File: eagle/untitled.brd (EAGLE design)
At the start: 50 x 50 mm, 48 parts, among them J1 JTAG, Q1 16MHz, U1 MMA3202KEG

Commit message: Update board.
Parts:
- removed D11: DIODE, gipi:1206
- removed G1: BAT, SparkFun-Electromechanical:BATTCOM_20MM_PTH
- added C7, C8, C9: 10nF, SparkFun-Capacitors:0603-CAP
- added D13: (no value), diode:SMB
- added JP6: M02JST-PTH-VERT, SparkFun-Connectors:JST-2-PTH-VERT
- added L1: (no value), SparkFun-Passives:0603
- added LED1: (no value), SparkFun-LED:LED-0603
- added R16, R17, R18: 1k, SparkFun-Passives:0603-RES
- added U$3: V_REG_TPS61040SMD, SparkFun-PowerIC:SOT23-5
- C1, C2, C3: device SparkFun-Capacitors:1206 -> SparkFun-Capacitors:0603-CAP
- C4, C5: value 10pF -> 10nF; device SparkFun-Capacitors:1206 -> SparkFun-Capacitors:0603-CAP
- GOLD_ORB_SM1: value OSHWLOGO_GOLD_ORB_SM -> OSHWLOGO_GOLD_ORB_LG; device bfl:OSHW2 -> bfl:OSHW0
- JP1: value M11PTH -> M13; device SparkFun-Connectors:1X11 -> SparkFun-Connectors:1X13
- R10, R3, R9: device SparkFun-Passives:1206 -> SparkFun-Passives:0603-RES
- moved J1 21.7 mm to (43.9, 75.4)
- moved C3 18.2 mm to (27.7, 75.5)
- moved U1 17.9 mm to (23.1, 73.4), flipped to the bottom, turned to 270 degrees
- moved JP5 14.4 mm to (9.75, 47.4), turned to 0 degrees
- moved GOLD_ORB_SM1 13.8 mm to (40.0, 46.0)
- moved SJ1 11.4 mm to (18.7, 72.9), turned to 270 degrees
- moved C5 11.2 mm to (30.1, 71.0), turned to 270 degrees
- moved JP2 10.9 mm to (5.29, 60.2)
- moved D12 9.81 mm to (11.9, 52.8), flipped to the bottom, turned to 180 degrees
- moved S1 8.30 mm to (4.40, 76.8)
- moved C6 8.06 mm to (13.2, 56.7)
- moved R9 7.30 mm to (27.9, 71.0)
- moved R1 6.33 mm to (13.2, 61.0)
- moved R2 6.29 mm to (13.3, 63.6)
- moved C4 4.13 mm to (25.7, 71.0), turned to 270 degrees
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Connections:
- removed net N$33: D11.P$1, G1.2
- new net GN: C4.1, C5.1, C6.2, D1.C, D2.C, D3.C, D4.C, D5.C, D6.C, D7.C, D8.C, D9.C, J1.10, J1.2, JP1.12, JP5.6, LED1.C, S1.1, S1.2, S2.3
- new net N$35: R16.1, U1.P$7
- new net N$36: LED1.A, R16.2
- new net N$38: C7.2, JP6.1, L1.1, U$3.4, U$3.5
- new net N$39: D13.A, L1.2, U$3.1
- new net N$41: C8.1, R17.1, R18.2, U$3.3
- new net N$42: C8.2, C9.2, D13.C, R17.2
- net GND-ISO: now also C7.1, C9.1, JP6.2, R18.1, U$3.2; no longer C4.1, C5.1, C6.2, D1.C, D2.C, D3.C, D4.C, D5.C, D6.C, D7.C, D8.C, D9.C, G1.1, J1.10, J1.2, JP5.6, S1.1, S1.2, S2.3
- net N$28: no longer D11.P$2
- net VCC1: now also JP1.13
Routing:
- net N$28: track 49.3 -> 13.0 mm
- net X: track 70.5 -> 36.6 mm
- net VCC2: track 48.0 -> 26.1 mm, vias 0 -> 1
- net N$17: track 78.2 -> 60.7 mm, vias 1 -> 0
- net N$42: track 0.00 -> 13.4 mm
- net N$21: track 24.3 -> 11.2 mm, vias 0 -> 1
- net GN: track 0.00 -> 12.7 mm, vias 0 -> 1
- net N$41: track 0.00 -> 12.6 mm
- net Y: track 37.3 -> 49.4 mm
- net N$27: track 11.2 -> 22.7 mm, vias 1 -> 0
- net VCC1: track 107.4 -> 118.7 mm
- net N$25: track 12.2 -> 23.3 mm, vias 1 -> 0
- net N$38: track 0.00 -> 10.7 mm
- net N$32: track 5.18 -> 15.6 mm, vias 0 -> 1
- net PD0: track 31.4 -> 39.9 mm, vias 2 -> 1
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- added copper zone on layer 1, net GN
- removed copper zone on layer 1, net GND-ISO
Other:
- board text removed: "+"
- board text removed: "-"
- board text removed: "PB0"
- board text removed: "PD1"
- board text removed: "PE6"

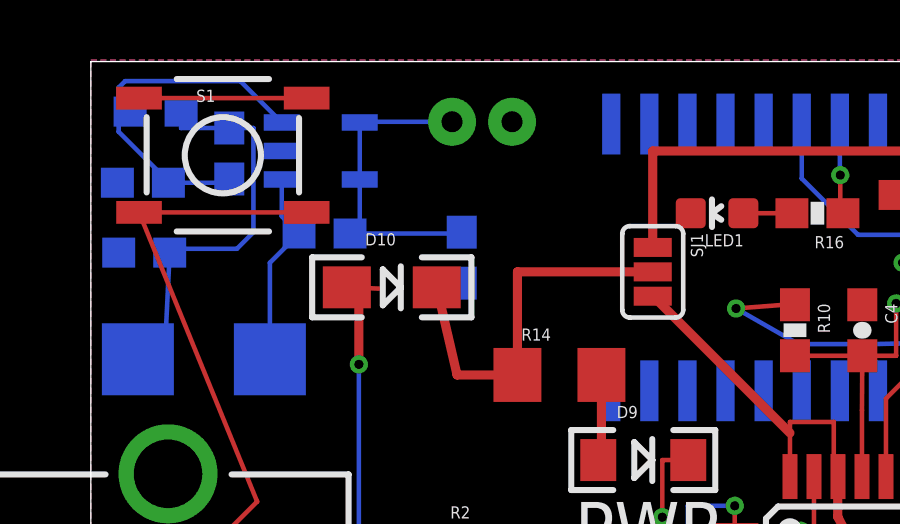
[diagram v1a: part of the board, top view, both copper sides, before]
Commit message: Add reverse voltage protection by P-MOSFET + Labelling.
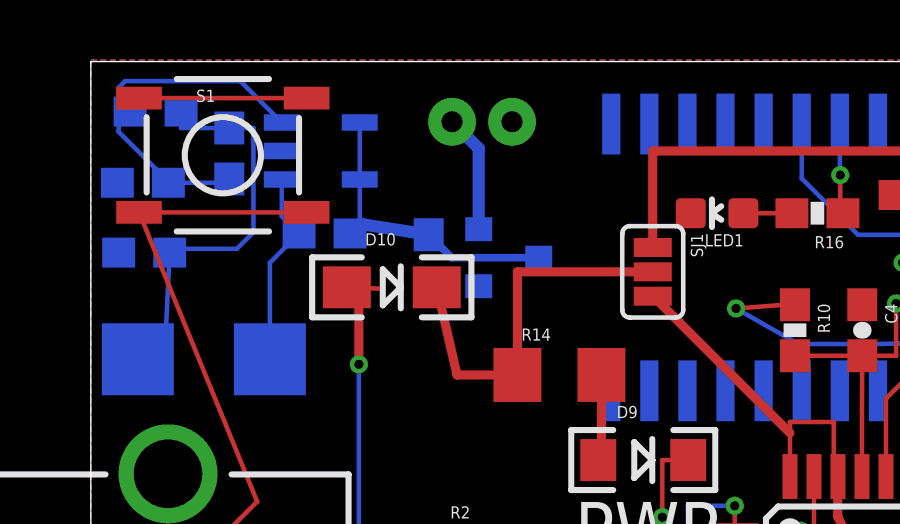
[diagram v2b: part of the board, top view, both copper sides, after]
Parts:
- added NFET: P-CHANNEL-MOSFET, GeekAmmo:SOT23-3
- moved C7 1.10 mm to (11.3, 73.3)
- renumbered U$3 to BOOST
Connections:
- new net N$33: JP6.1, NFET.2
- net GND-ISO: now also NFET.1
- net N$38: now also NFET.3; no longer JP6.1
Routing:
- net N$33: track 0.00 -> 3.95 mm
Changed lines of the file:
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@@
 <layer number="19" name="Unrouted" color="2" fill="1" visible="yes" active="yes"/>
 <layer number="20" name="Dimension" color="15" fill="1" visible="yes" active="yes"/>
-<layer number="21" name="tPlace" color="7" fill="1" visible="no" active="yes"/>
+<layer number="21" name="tPlace" color="7" fill="1" visible="yes" active="yes"/>
 <layer number="22" name="bPlace" color="15" fill="1" visible="yes" active="yes"/>
-<layer number="23" name="tOrigins" color="15" fill="1" visible="no" active="yes"/>
+<layer number="23" name="tOrigins" color="15" fill="1" visible="yes" active="yes"/>
 <layer number="24" name="bOrigins" color="15" fill="1" visible="yes" active="yes"/>
 <layer number="25" name="tNames" color="7" fill="1" visible="no" active="yes"/>
@@
 <element name="R16" library="SparkFun-Passives" package="0603-RES" value="1k" x="24.219509375" y="74.90264375" rot="R180"/>
 <element name="LED1" library="SparkFun-LED" package="LED-0603" value="" x="20.874509375" y="74.90264375" rot="R90"/>
-<element name="U$3" library="SparkFun-PowerIC" package="SOT23-5" value="V_REG_TPS61040SMD" x="7.663865625" y="76.977390625" rot="MR90"/>
+<element name="BOOST" library="SparkFun-PowerIC" package="SOT23-5" value="V_REG_TPS61040SMD" x="7.663865625" y="76.977390625" smashed="yes" rot="MR90">
+<attribute name="NAME" x="7.918346875" y="78.1627875" size="0.508" layer="26" font="vector" ratio="16" rot="MR270"/>
+<attribute name="VALUE" x="7.473365625" y="76.024890625" size="0.4064" layer="28" rot="MR90"/>
+</element>
 <element name="L1" library="SparkFun-Passives" package="0603" value="" x="7.790896875" y="74.225184375" smashed="yes" rot="MR0">
 <attribute name="NAME" x="8.8492625" y="72.5737" size="1.016" layer="26" font="vector" ratio="16" rot="MR0"/>
 <attribute name="VALUE" x="8.806896875" y="73.082184375" size="0.4064" layer="28" font="vector" rot="MR0"/>
 </element>
-<element name="C7" library="SparkFun-Capacitors" package="0603-CAP" value="10nF" x="12.363809375" y="73.420675" rot="MR90"/>
+<element name="C7" library="SparkFun-Capacitors" package="0603-CAP" value="10nF" x="11.262925" y="73.335990625" rot="MR90"/>
 <element name="D13" library="diode" package="SMB" value="" x="3.7684125" y="70.033334375" rot="MR180"/>
 <element name="R17" library="SparkFun-Passives" package="0603-RES" value="1k" x="2.15943125" y="78.28999375" rot="MR180"/>
@@
 <element name="C9" library="SparkFun-Capacitors" package="0603-CAP" value="10nF" x="1.778353125" y="73.59004375" rot="MR180"/>
 <element name="JP6" library="SparkFun-Connectors" package="JST-2-PTH-VERT" value="M02JST-PTH-VERT" x="13.041275" y="77.4008125" rot="MR180"/>
+<element name="NFET" library="GeekAmmo" package="SOT23-3" value="P-CHANNEL-MOSFET" x="13.93045" y="73.42068125" rot="MR90"/>
 </elements>
 <signals>
@@
 <signal name="N$38">
 <contactref element="L1" pad="1"/>
-<contactref element="U$3" pad="5"/>
-<contactref element="U$3" pad="4"/>
+<contactref element="BOOST" pad="5"/>
+<contactref element="BOOST" pad="4"/>
 <contactref element="C7" pad="2"/>
-<contactref element="JP6" pad="1"/>
 <wire x1="8.963965625" y1="77.927390625" x2="8.963965625" y2="76.027390625" width="0.1524" layer="16"/>
 <wire x1="8.640896875" y1="74.225184375" x2="8.963965625" y2="74.548253125" width="0.1524" layer="16"/>
 <wire x1="8.963965625" y1="74.548253125" x2="8.963965625" y2="76.027390625" width="0.1524" layer="16"/>
 <wire x1="8.963965625" y1="77.927390625" x2="8.9873875" y2="77.9508125" width="0.1524" layer="16"/>
-<wire x1="8.9873875" y1="77.9508125" x2="12.041275" y2="77.9508125" width="0.1524" layer="16"/>
-<wire x1="12.363809375" y1="74.270675" x2="12.31831875" y2="74.225184375" width="0.1524" layer="16"/>
-<wire x1="12.31831875" y1="74.225184375" x2="8.640896875" y2="74.225184375" width="0.1524" layer="16"/>
+<contactref element="NFET" pad="3"/>
+<wire x1="8.963965625" y1="74.548253125" x2="11.262925" y2="74.185990625" width="0.4064" layer="16"/>
+<wire x1="11.262925" y1="74.185990625" x2="12.028234375" y2="73.42068125" width="0.254" layer="16"/>
+<wire x1="12.028234375" y1="73.42068125" x2="14.93045" y2="73.42068125" width="0.254" layer="16"/>
 </signal>
 <signal name="N$39">
 <contactref element="L1" pad="2"/>
-<contactref element="U$3" pad="1"/>
+<contactref element="BOOST" pad="1"/>
 <contactref element="D13" pad="A"/>
 <wire x1="6.940896875" y1="74.225184375" x2="6.363765625" y2="74.802315625" width="0.1524" layer="16"/>
@@
 <signal name="GND-ISO">
 <contactref element="C7" pad="1"/>
-<contactref element="U$3" pad="2"/>
+<contactref element="BOOST" pad="2"/>
 <contactref element="R18" pad="1"/>
 <contactref element="C9" pad="1"/>
@@
 <wire x1="26.8083375" y1="75.511053125" x2="28.43295" y2="73.886440625" width="0.1524" layer="1"/>
 <wire x1="28.43295" y1="73.886440625" x2="28.707740625" y2="73.886440625" width="0.1524" layer="1"/>
+<contactref element="NFET" pad="1"/>
 </signal>
 <signal name="N$41">
-<contactref element="U$3" pad="3"/>
+<contactref element="BOOST" pad="3"/>
 <contactref element="R18" pad="2"/>
 <contactref element="R17" pad="1"/>
@@
 <wire x1="3.00943125" y1="77.742709375" x2="4.6152625" y2="77.742709375" width="0.1524" layer="16"/>
 </signal>
+<signal name="N$33">
+<contactref element="JP6" pad="1"/>
+<contactref element="NFET" pad="2"/>
+<wire x1="12.041275" y1="77.9508125" x2="12.93045" y2="77.0616375" width="0.4064" layer="16"/>
+<wire x1="12.93045" y1="77.0616375" x2="12.93045" y2="74.37068125" width="0.4064" layer="16"/>
+</signal>
 </signals>

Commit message: Rework labels.
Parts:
- D13: value (none) -> DIODE; device diode:SMB -> gipi:1206
- turned D13 to 0 degrees
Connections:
- net N$39: now also D13.P$1; no longer D13.A
- net N$42: now also D13.P$2; no longer D13.C
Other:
- board text added: "RESET"

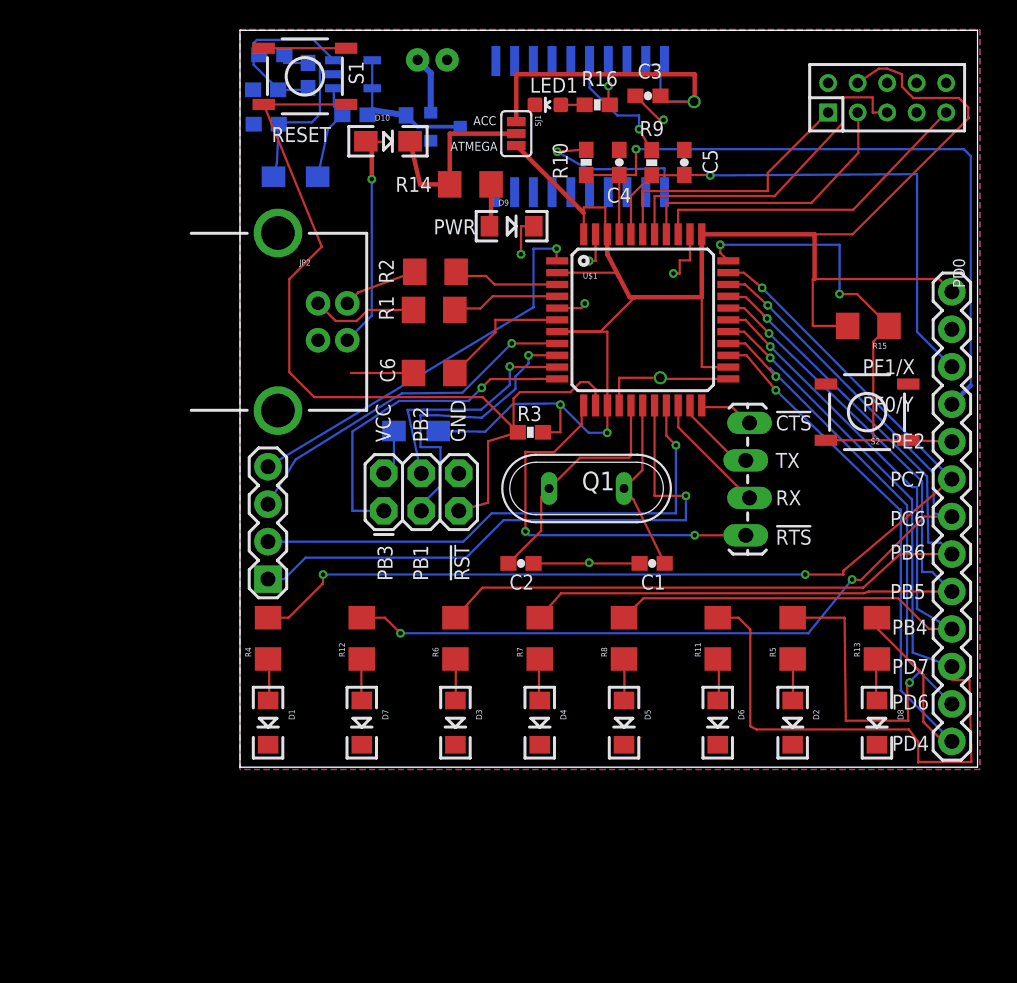
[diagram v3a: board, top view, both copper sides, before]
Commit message: Fix board layout.
Done some rerouting.
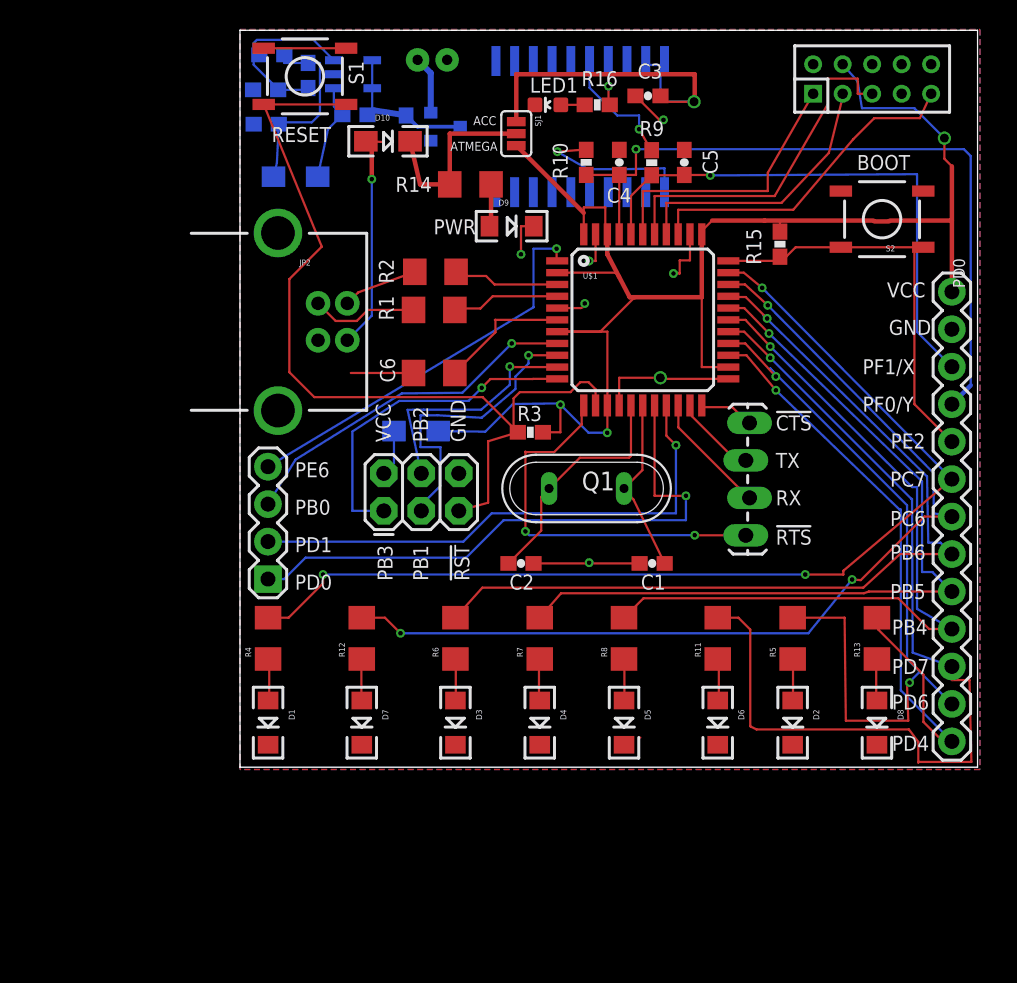
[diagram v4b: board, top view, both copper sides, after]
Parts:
- R15: device SparkFun-Passives:1206 -> SparkFun-Passives:0603-RES
- moved S2 13.1 mm to (43.5, 67.2)
- moved R15 8.16 mm to (36.6, 65.5), turned to 90 degrees
- moved J1 1.63 mm to (42.9, 76.7)
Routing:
- net VCC1: track 118.7 -> 108.7 mm, vias 2 -> 3
- net PE2: track 33.7 -> 28.0 mm, vias 2 -> 0
- net N$26: track 19.4 -> 18.8 mm
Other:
- board text added: "BOOT"
- board text added: "PB0"
- board text added: "PD1"
- board text added: "PE6"

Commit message: Rework some traces.
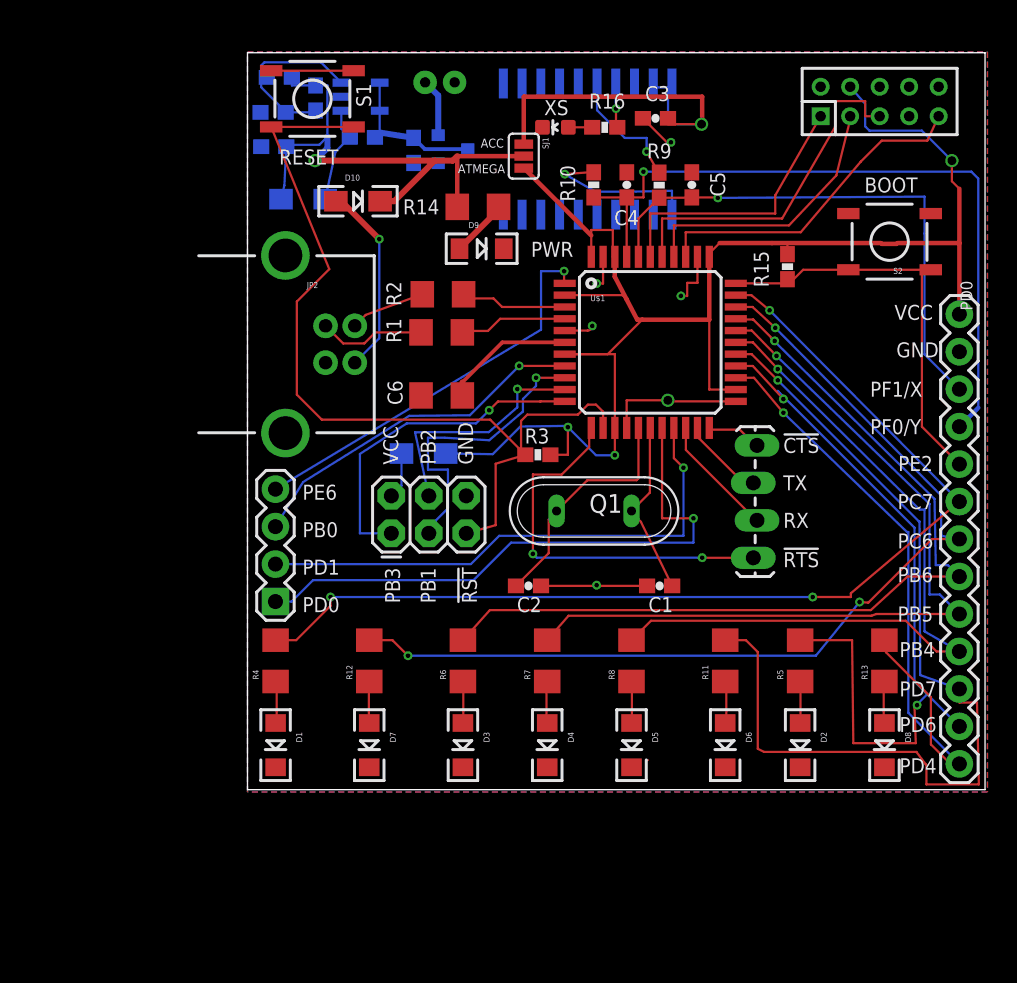
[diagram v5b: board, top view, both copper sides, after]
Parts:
- removed LED1: (no value), SparkFun-LED:LED-0603
- added XS: (no value), SparkFun-LED:LED-0603
- moved D10 4.54 mm to (8.00, 68.4)
- moved D9 2.54 mm to (16.4, 65.2)
- moved D6 1.61 mm to (32.9, 31.5)
- moved D8 1.61 mm to (43.7, 31.5)
- moved D1 1.61 mm to (2.41, 31.5)
- moved D3 1.61 mm to (15.1, 31.5)
- moved D4 1.61 mm to (20.8, 31.5)
- moved D5 1.61 mm to (26.5, 31.5)
- moved D7 1.61 mm to (8.76, 31.5)
- moved D2 1.61 mm to (38.0, 31.5)
- moved C3 1.61 mm to (28.2, 74.0)
- moved C4 1.61 mm to (26.2, 69.5)
- moved GOLD_ORB_SM1 1.61 mm to (40.5, 44.5)
- moved JP1 1.61 mm to (48.8, 30.2)
- moved JP4 1.61 mm to (34.8, 44.2)
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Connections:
- removed net N$28: D10.P$2, R14.1, SJ1.2
- removed net N$42: C8.2, C9.2, D13.P$2, R17.2
- new net VBATT: C8.2, C9.2, D10.P$2, D13.P$2, R14.1, R17.2, SJ1.2
- net GN: now also XS.C; no longer LED1.C
- net N$36: now also XS.A; no longer LED1.A
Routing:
- net VBATT: track 0.00 -> 37.6 mm, vias 0 -> 1
- net N$42: track 13.1 -> 0.00 mm
- net N$28: track 13.0 -> 0.00 mm
- net GN: track 12.7 -> 5.72 mm, vias 1 -> 0
- net N$32: track 15.6 -> 13.1 mm
- net N$18: track 2.94 -> 3.93 mm

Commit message: Modified some trace's widths.
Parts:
- moved R17 0.36 mm to (2.41, 77.0)
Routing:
- net PE6: track 27.4 -> 25.4 mm
- net VCC1: track 108.8 -> 107.7 mm

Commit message: Fix label mosfet.
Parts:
- renumbered NFET to N-FET
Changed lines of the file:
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@@
 <attribute name="VALUE" x="15.565275" y="72.8768125" size="0.4064" layer="28" rot="MR180"/>
 </element>
-<element name="NFET" library="GeekAmmo" package="SOT23-3" value="P-CHANNEL-MOSFET" x="14.43845" y="71.89668125" rot="MR90"/>
+<element name="N-FET" library="GeekAmmo" package="SOT23-3" value="P-CHANNEL-MOSFET" x="14.43845" y="71.89668125" smashed="yes" rot="MR90">
+<attribute name="NAME" x="16.11431875" y="68.66745" size="1.27" layer="26" ratio="16" rot="MR0"/>
+<attribute name="VALUE" x="11.26345" y="69.99168125" size="1.27" layer="28" rot="MR90"/>
+</element>
 </elements>
 <signals>
@@
 <wire x1="9.471965625" y1="73.024253125" x2="9.471965625" y2="74.503390625" width="0.1524" layer="16"/>
 <wire x1="9.471965625" y1="76.403390625" x2="9.4953875" y2="76.4268125" width="0.1524" layer="16"/>
-<contactref element="NFET" pad="3"/>
+<contactref element="N-FET" pad="3"/>
 <wire x1="9.471965625" y1="73.024253125" x2="11.770925" y2="72.661990625" width="0.4064" layer="16"/>
 <wire x1="11.770925" y1="72.661990625" x2="12.536234375" y2="71.89668125" width="0.254" layer="16"/>
@@
 <wire x1="27.3163375" y1="73.987053125" x2="28.94095" y2="72.362440625" width="0.1524" layer="1"/>
 <wire x1="28.94095" y1="72.362440625" x2="29.215740625" y2="72.362440625" width="0.1524" layer="1"/>
-<contactref element="NFET" pad="1"/>
+<contactref element="N-FET" pad="1"/>
 <wire x1="31.013" y1="64.601" x2="31.013" y2="61.946359375" width="0.508" layer="1"/>
 <wire x1="31.013" y1="61.946359375" x2="29.893209375" y2="61.946359375" width="0.508" layer="1"/>
@@
 <signal name="N$33">
 <contactref element="JP6" pad="1"/>
-<contactref element="NFET" pad="2"/>
+<contactref element="N-FET" pad="2"/>
 <wire x1="12.549275" y1="76.4268125" x2="13.43845" y2="75.5376375" width="0.4064" layer="16"/>
 <wire x1="13.43845" y1="75.5376375" x2="13.43845" y2="72.84668125" width="0.4064" layer="16"/>
